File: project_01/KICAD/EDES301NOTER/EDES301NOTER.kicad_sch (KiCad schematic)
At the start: 39 parts, among them Q1 S8050, Q2 BSS84, Q3 BSS84, Q4 BSS84, Q5 BSS138, Q7 BSS138, SW1 SW_Reed, U1 POCKETBEAGLE, U3 TPS613222ADBVR

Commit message: UpdateSchematicV1
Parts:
- removed SW1: SW_Reed, symbol Switch:SW_Reed
- added C12, C13: 1uF, Footprints:CAPC1608X90N, symbol Device:C
- added Q6: BSS84, Package_TO_SOT_SMD:SOT-23, symbol Transistor_FET:BSS84
- added R15, R16: 100k, Footprints:RESC1607X60N, symbol Device:R
- added U2: DRV5032FCDBZR, DBZ0003A-IPC_A, symbol DRV5032FCDBZR:DRV5032FCDBZR
- added U7: MMBD4148-7-F, SOT-23_DIO, symbol MMBD4148-7-F:MMBD4148-7-F
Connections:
- net +3.3V: now also Q5.1 (G), Q7.1 (G), R10.1, R12.1, R14.1, C12.1, U2.1 (VCC); no longer R14.2
- net +3.3VA: no longer Q5.1 (G), Q7.1 (G), R10.1, R12.1, U1.14 (3.3V@1)
- net -BATT: now also C12.2, Q6.2 (S), R16.1, U2.3 (GND), U7.2 (EPAD); no longer U1.22 (GND@3)
- net DATA: now also Q7.3 (D), R13.2, U4.3 (SDA); no longer Q5.2 (S), Q7.2 (S), R10.2, R12.2, U1.10 (SPI0.MISO), U1.12 (SPI0.MOSI), U1.45 (I2C1.SCL), U1.47 (I2C1.SDA), U1.6 (SPI0.CS), U1.61 (SPI1.MOSI), U1.65 (SPI1.CLK), U1.67 (SPI1.CS), U1.8 (SPI0.CLK), U5.3 (SCL), U5.5 (CSX), U5.6 (SDA), U5.7 (SDO), U6.3 (SDI), U6.4 (SCLK), U6.5 (CS)
- net at U1.38 (GPIO59): no longer R14.1
- net EPPR_PWR: now reaches Q4.1 (G), R9.1
- net EPPR_PWR: now also U1.58 (GPIO46); no longer U1.56 (GPIO64)
- net at U1.53 (GPIO65): no longer U6.6 (D/C)
- net EPPR_RST: now reaches U1.69 (GPIO45), U6.7 (RES)
- net EPPR_BUSY: now reaches U1.34 (GPIO26), U6.8 (BUSY)
- net TFT_BL: now reaches R5.2, U1.37 (PWM1A)
- net TFT_BL: now also Q3.1 (G), R8.1
- net BATT_TEMP: now reaches TH1.2, U1.52 (BAT.TEMP)
- net BOOST_PWR: now reaches Q2.1 (G), R7.1
- net BOOST_PWR: now also U1.60 (GPIO44); no longer U1.44 (GPIO60)
- net TFT_D/C: now reaches U1.2 (AIN6/GPIO87), U5.4 (D/C)
- net TFT_RST: now reaches U1.39 (GPIO23), U5.2 (RESET)
- net PB_PWR: now reaches U1.48 (PWR.BTN)
- net PB_PWR: now also Q6.3 (D)
- net EPPR_D/C: now reaches U1.54 (GPIO47)
- net EPPR_D/C: now also U6.6 (D/C)
- net PB_LID: now reaches U1.55 (GPIO27)
- net PB_LID: now also R14.2, C13.1, U2.2 (OUT)
- net PWM_BL_CTR: no longer names the net of Q1.2 (B), R5.1, R6.1
- new net: R15.2, R16.2
- new net: C13.2, Q6.1 (G), R15.1, U7.1 (EPAD)
- new net CARD_SCL: Q5.2 (S), R10.2, U1.45 (I2C1.SCL)
- new net CARD_SDA: Q7.2 (S), R12.2, U1.47 (I2C1.SDA)
- new net EPPR_CLK: U1.65 (SPI1.CLK), U6.4 (SCLK)
- new net EPPR_CS: U1.67 (SPI1.CS), U6.5 (CS)
- new net EPPR_MISO: U1.61 (SPI1.MOSI), U6.3 (SDI)
- new net TFT_CSX: U1.6 (SPI0.CS), U5.5 (CSX)
- new net TFT_PWR: U1.20 (GPIO20)
- new net TFT_SDA: U1.12 (SPI0.MOSI), U5.6 (SDA)
- new net TFT_SDL: U1.8 (SPI0.CLK), U5.3 (SCL)
- new net TFT_SDO: U1.10 (SPI0.MISO), U5.7 (SDO)
- no-connect marks 0 -> 1
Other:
- moved on the sheet: C6, C8, C9, L1, Q1, Q4, R5, R6, R9

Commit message: updateschemv1
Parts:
- removed TH1: Thermistor_NTC, symbol Device:Thermistor_NTC
- added RT1: NXRT15XH103FA1B040, NXRT15XH103FA1B040:THERM_NXRT15XH103FA1B040, symbol NXRT15XH103FA1B040:NXRT15XH103FA1B040
- U4: footprint (none) -> Connector:4_Wire_Header__2_54mm
- U5: footprint (none) -> 18PinFPC0_5mm 5034801800:CON_5034801800_MOL
- U7: footprint SOT-23_DIO -> Package_TO_SOT_SMD:SOT-23
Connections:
- net +5V: now also C8.1, U4.1 (5V); no longer C8.2, U4.2 (5V)
- net -BATT: now also C8.2, U4.4 (GND), RT1.2; no longer C8.1, U4.1 (GND)
- net BATT_TEMP: now also RT1.1
- net DATA: now also U4.2 (SDA); no longer U4.4 (SCL)
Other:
- moved on the sheet: C8

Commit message: SchemV2.2
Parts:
- removed C1, C10, C11, C2: 10uF, Footprints:CAPC1608X90N, symbol Device:C
- removed C12, C13, C7, C8, C9: 1uF, Footprints:CAPC1608X90N, symbol Device:C
- removed C3, C5, C6: 0.1uF, Footprints:CAPC1608X90, symbol Device:C
- removed L1: 2.2uH, Footprints:IND_VLS252012ET-2R2M, symbol Device:L
- removed Q1: S8050, Package_TO_SOT_THT:TO-92_Inline, symbol Transistor_BJT:S8050
- removed Q2, Q3, Q4, Q6: BSS84, Package_TO_SOT_SMD:SOT-23, symbol Transistor_FET:BSS84
- removed Q5, Q7: BSS138, Footprints:SOT95P240X111-3N, symbol Transistor_FET:BSS138
- removed R1, R2, R3, R4: 10R, Footprints:RESC2012X60N, symbol Device:R
- removed R10, R11, R12, R13, R14: 10k, Footprints:RESC1607X60N, symbol Device:R
- removed R15, R16, R7, R8, R9: 100k, Footprints:RESC1607X60N, symbol Device:R
- removed R5, R6: 1K, Footprints:RESC1607X60N, symbol Device:R
- removed U2: DRV5032FCDBZR, DBZ0003A-IPC_A, symbol DRV5032FCDBZR:DRV5032FCDBZR
- removed U3: TPS613222ADBVR, TPS613222ADBVR:SOT95P280X145-5N, symbol TPS613222ADBVR:TPS613222ADBVR
- removed U4: ~, Connector:4_Wire_Header__2_54mm, symbol STIKE:CARDKB
- removed U5: ~, 18PinFPC0_5mm 5034801800:CON_5034801800_MOL, symbol YT280S010:DISPLAY
- removed U6: ~, symbol EPAPER:DESPI-C02
- removed U7: MMBD4148-7-F, Package_TO_SOT_SMD:SOT-23, symbol MMBD4148-7-F:MMBD4148-7-F
- C4: value C -> 47uF
- RT1: footprint NXRT15XH103FA1B040:THERM_NXRT15XH103FA1B040 -> HomeBrew:2_Wire_Connector
- U1: footprint POCKETBEAGLE:POCKETBEAGLE -> POCKETBEAGLE (1):POCKETBEAGLE
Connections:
- net +3.3VA is gone; now on net -BATT: C4.1
- net +3.3V: now also C4.2, U1.59 (3.3V@2)
- no-connect marks 1 -> 0
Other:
- added sheet 5V Boost Converter (Boost5V.kicad_sch)
- added sheet CardKB (CardKB.kicad_sch)
- added sheet Hall Effect Power Switch (HallSwitch.kicad_sch)
- added sheet TFT Display (TFTDisp.kicad_sch)
- added sheet ePaper Support Circuit (ePaperSupport.kicad_sch)
- note removed: "(NO)Low Power Switch"
- note removed: "3.3V to 5V Logic Level Shifter"
- note removed: "Toggle-able Boost Converter (Quieted)"
- moved on the sheet: C4, RT1, U1

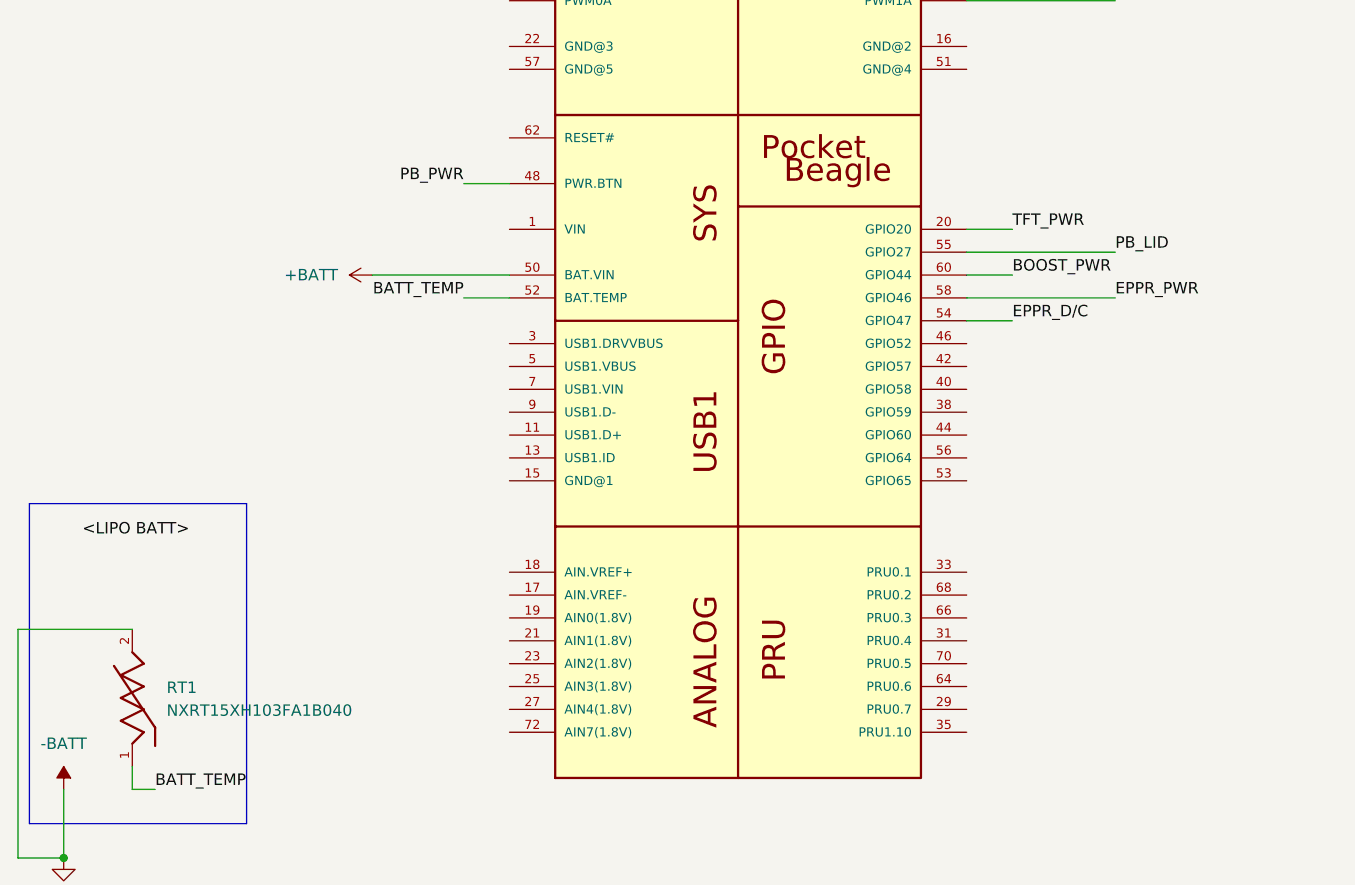
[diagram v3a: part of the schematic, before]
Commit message: SchematicV2UploadPDF
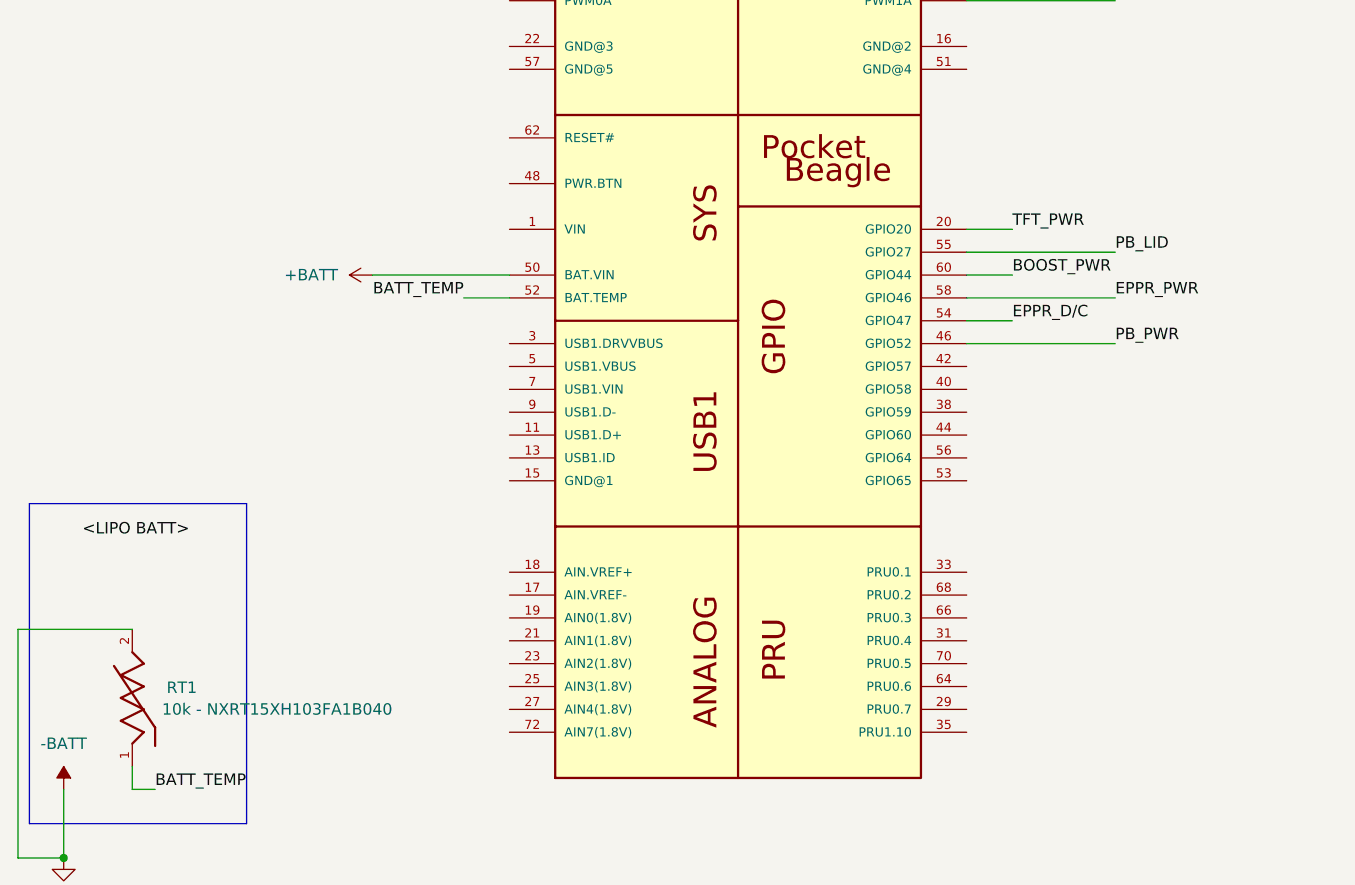
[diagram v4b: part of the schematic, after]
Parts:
- RT1: value NXRT15XH103FA1B040 -> 10k - NXRT15XH103FA1B040
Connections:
- net PB_PWR: now also U1.46 (GPIO52); no longer U1.48 (PWR.BTN)
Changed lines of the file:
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@@
-	(wire
-		(pts
-			(xy 93.98 113.03) (xy 99.06 113.03)
-		)
-		(stroke
-			(width 0)
-			(type default)
-		)
-	)
 	(wire
 		(pts
@@
 		(pts
 			(xy 149.86 92.71) (xy 166.37 92.71)
+		)
+		(stroke
+			(width 0)
+			(type default)
+		)
+	)
+	(wire
+		(pts
+			(xy 149.86 130.81) (xy 166.37 130.81)
 		)
 		(stroke
@@
 		)
 	)
-	(label "PB_PWR"
-		(at 93.98 113.03 180)
-		(fields_autoplaced yes)
-		(effects
-			(font
-				(size 1.27 1.27)
-			)
-			(justify right bottom)
-		)
-		(property "Netclass" "DATA"
-			(at 93.98 114.3 0)
-			(effects
-				(font
-					(size 1.27 1.27)
-					(italic yes)
-				)
-				(justify right)
-			)
-		)
-	)
 	(label "EPPR_MISO"
 		(at 95.25 69.85 180)
@@
 		(property "Netclass" "DATA"
 			(at 166.37 73.66 0)
+			(effects
+				(font
+					(size 1.27 1.27)
+					(italic yes)
+				)
+				(justify left)
+			)
+		)
+	)
+	(label "PB_PWR"
+		(at 166.37 130.81 0)
+		(fields_autoplaced yes)
+		(effects
+			(font
+				(size 1.27 1.27)
+			)
+			(justify left bottom)
+		)
+		(property "Netclass" "DATA"
+			(at 166.37 132.08 0)
 			(effects
 				(font
@@
 		(on_board yes)
 		(dnp no)
-		(fields_autoplaced yes)
 		(property "Reference" "RT1"
 			(at 60.96 169.0369 90)
@@
 			)
 		)
-		(property "Value" "NXRT15XH103FA1B040"
-			(at 60.96 171.5769 90)
-			(effects
-				(font
+		(property "Value" "10k - NXRT15XH103FA1B040"
+			(at 60.452 171.45 90)
+			(effects
+				(font

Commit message: Revise Boost5V schematic and add STIKE symbols
Refactor Boost5V.kicad_sch: updated title block and paper size, reorganized and renamed many symbol definitions (capacitor/inductor/diode/resistor/LED/driver), adjusted pin assignments, footprints, datasheet links and symbol graphics. Added new STIKE-related schematic symbols (Slide Switch, LipoConnection) and multiple KiCad footprint/symbol files under KICAD Files. Added project backup zips and freerouting.dsn, removed a temporary .kicad_sch.lck, and updated project metadata files (.kicad_pcb, .kicad_prl, .kicad_pro, .kicad_sch).
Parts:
- removed C4: 47uF, Footprints:CAPC2012X145N, symbol Device:C
- removed RT1: 10k - NXRT15XH103FA1B040, HomeBrew:2_Wire_Connector, symbol NXRT15XH103FA1B040:NXRT15XH103FA1B040
- removed U1: POCKETBEAGLE, POCKETBEAGLE (1):POCKETBEAGLE, symbol POCKETBEAGLE:POCKETBEAGLE
- added C9: 1uF, Capacitor_SMD:C_0603_1608Metric_Pad1.08x0.95mm_HandSolder, symbol Device:C_Small
- added SW1: Boot, STIKE:MembraneButton, symbol STIKE:MembraneButton
- added SW2: RST, STIKE:MembraneButton, symbol STIKE:MembraneButton
- added U4: ~, HomeBrew:4_Wire_Connector, symbol STIKE:CARDKB
- added U7: ~, STIKE:THROUGH8, symbol STIKE:ePaper
- added U8: ~, STIKE:THROUGH8, symbol STIKE:LCD
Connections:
- net +3.3V: now also U7.8 (3.3V), U8.2 (3.3V)
- new net +5V: C9.1, U4.2 (5V)
- new net ESP32-S3-N16R8/BOOT: SW1.1
- new net ESP32-S3-N16R8/EP_BUSY: U7.1 (EP_BUSY)
- new net ESP32-S3-N16R8/EP_CS: U7.4 (EP_CS)
- new net ESP32-S3-N16R8/EP_DC: U7.3 (EP_DC)
- new net ESP32-S3-N16R8/EP_MOSI: U7.6 (EP_SDI)
- new net ESP32-S3-N16R8/EP_RST: U7.2 (EP_RES)
- new net ESP32-S3-N16R8/EP_SCK: U7.5 (EP_SCK)
- new net ESP32-S3-N16R8/LCD_BL: U8.8 (LCD_BL)
- new net ESP32-S3-N16R8/LCD_CS: U8.7 (LCD_CS)
- new net ESP32-S3-N16R8/LCD_DC: U8.6 (LCD_DC)
- new net ESP32-S3-N16R8/LCD_MOSI: U8.4 (LCD_MOSI)
- new net ESP32-S3-N16R8/LCD_RST: U8.5 (LCD_RST)
- new net ESP32-S3-N16R8/LCD_SCK: U8.3 (LCD_SCK)
- new net ESP32-S3-N16R8/RST: SW2.1
- new net GND: C9.2, SW1.3, SW2.3, U4.1 (GND), U7.7 (GND), U8.1 (GND)
- new net LogicLevelConverter/HV1: U4.3 (SDA)
- new net LogicLevelConverter/HV2: U4.4 (SCL)
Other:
- sheet 5V Boost Converter renamed Power Circuitry
- sheet CardKB renamed LogicLevelConverter
- removed sheet Hall Effect Power Switch
- removed sheet TFT Display
- removed sheet ePaper Support Circuit
- added sheet ESP32-S3-N16R8 (STIKE-ESP32.kicad_sch)
- added sheet USBC-CONN (STIKE-USB.kicad_sch)
- sheet LogicLevelConverter ports: added HV1, HV2, LV1, LV2; removed none
- sheet Power Circuitry ports: added PB_LID; removed none
- title: STIK-eNOTE -> STIK eNote
